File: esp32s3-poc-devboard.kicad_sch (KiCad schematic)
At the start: 12 parts, among them U1 ESP32-S3, U2 AMS1117-3.3, U3 XC6206P332MR

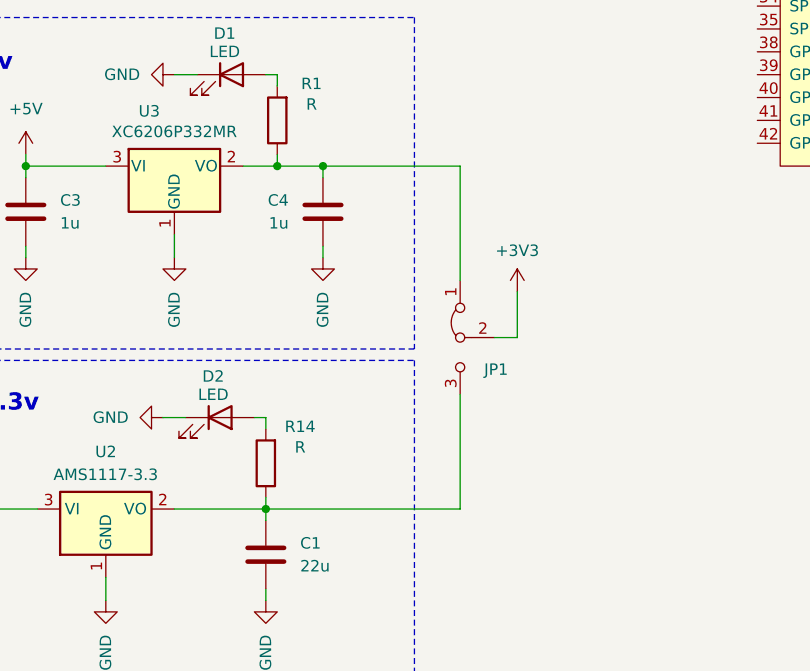
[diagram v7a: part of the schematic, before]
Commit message: remove 3v3 jumper
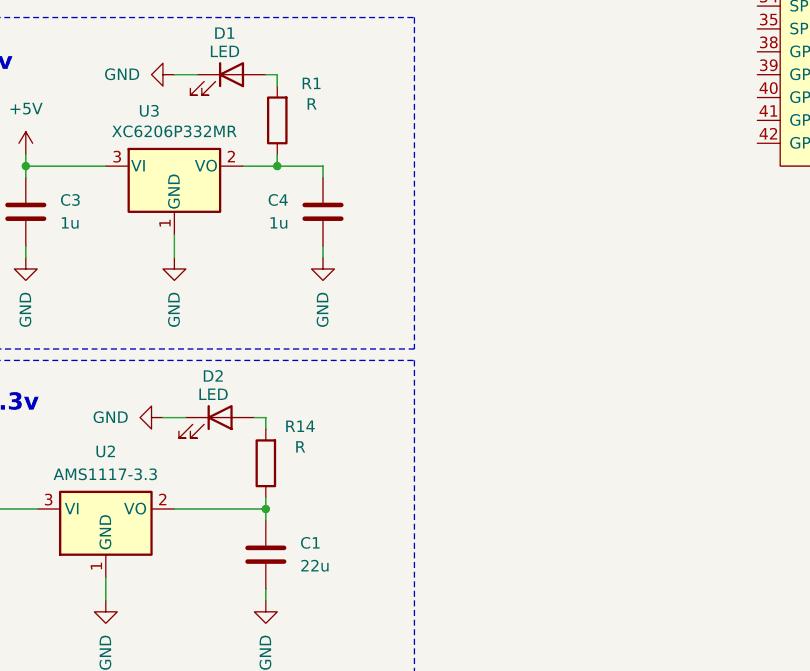
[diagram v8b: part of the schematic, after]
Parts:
- removed JP1: PWR, symbol Jumper:Jumper_3_Bridged12
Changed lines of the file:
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@@
-	)
-	(junction
-		(at 72.39 135.89)
-		(diameter 0)
-		(color 0 0 0 0)
 	)
 	(junction
@@
 	(wire
 		(pts
-			(xy 91.44 154.94) (xy 93.98 154.94)
-		)
-		(stroke
-			(width 0)
-			(type default)
-		)
-	)
-	(wire
-		(pts
-			(xy 93.98 154.94) (xy 93.98 149.86)
-		)
-		(stroke
-			(width 0)
-			(type default)
-		)
-	)
-	(wire
-		(pts
 			(xy 66.04 173.99) (xy 66.04 175.26)
 		)
@@
 	(wire
 		(pts
-			(xy 87.63 148.59) (xy 87.63 135.89)
-		)
-		(stroke
-			(width 0)
-			(type default)
-		)
-	)
-	(wire
-		(pts
 			(xy 29.21 175.26) (xy 29.21 173.99)
 		)
@@
 	(wire
 		(pts
-			(xy 66.04 173.99) (xy 87.63 173.99)
-		)
-		(stroke
-			(width 0)
-			(type default)
-		)
-	)
-	(wire
-		(pts
 			(xy 66.04 125.73) (xy 67.31 125.73)
 		)
@@
 	(wire
 		(pts
-			(xy 72.39 135.89) (xy 87.63 135.89)
-		)
-		(stroke
-			(width 0)
-			(type default)
-		)
-	)
-	(wire
-		(pts
 			(xy 55.88 125.73) (xy 58.42 125.73)
 		)
@@
 		(pts
 			(xy 29.21 173.99) (xy 40.64 173.99)
-		)
-		(stroke
-			(width 0)
-			(type default)
-		)
-	)
-	(wire
-		(pts
-			(xy 87.63 173.99) (xy 87.63 161.29)
 		)
 		(stroke
@@
 	)
 	(symbol
-		(lib_id "Jumper:Jumper_3_Bridged12")
-		(at 87.63 154.94 90)
-		(mirror x)
-		(unit 1)
-		(exclude_from_sim no)
-		(in_bom no)
-		(on_board yes)
-		(dnp no)
-		(property "Reference" "JP1"
-			(at 92.964 158.496 90)
-			(effects
-				(font
-					(size 1.27 1.27)
-				)
-				(justify left)
-			)
-		)
-		(property "Value" "PWR"
-			(at 92.456 159.766 90)
-			(effects
-				(font
-					(size 1.27 1.27)
-				)
-				(justify left)
-				(hide yes)
-			)
-		)
-		(property "Footprint" ""
-			(at 87.63 154.94 0)
-			(effects
-				(font
-					(size 1.27 1.27)
-				)
-				(hide yes)
-			)
-		)
-		(property "Datasheet" "~"
-			(at 87.63 154.94 0)
-			(effects
-				(font
-					(size 1.27 1.27)
-				)
-				(hide yes)
-			)
-		)
-		(property "Description" "Jumper, 3-pole, pins 1+2 closed/bridged"
-			(at 87.63 154.94 0)
-			(effects
-				(font
-					(size 1.27 1.27)
-				)
-				(hide yes)
-			)
-		)
-		(pin "3"
-		)
-		(pin "2"
-		)
-		(pin "1"
-		)
-		(instances
-			(project ""
-				(path "/a6beb550-83d0-4746-bc61-cde76b7466a3"
-					(reference "JP1")
-					(unit 1)
-				)
-			)
-		)
-	)
-	(symbol
 		(lib_id "Device:R")
 		(at 66.04 168.91 180)
@@
 					(unit 1)
 				)
-			)
-		)
-	)
-	(symbol
-		(lib_id "power:+3V3")
-		(at 93.98 149.86 0)
-		(mirror y)
-		(unit 1)
-		(exclude_from_sim no)
-		(in_bom yes)
-		(on_board yes)
-		(dnp no)
-		(property "Reference" "#PWR023"
-			(at 93.98 153.67 0)
-			(effects
-				(font
-					(size 1.27 1.27)
-				)
-				(hide yes)
-			)
-		)
-		(property "Value" "+3V3"
-			(at 93.98 145.288 0)
-			(effects
-				(font
-					(size 1.27 1.27)
-				)
-			)
-		)
-		(property "Footprint" ""
-			(at 93.98 149.86 0)
-			(effects
-				(font
-					(size 1.27 1.27)
-				)
-				(hide yes)
-			)
-		)
-		(property "Datasheet" ""
-			(at 93.98 149.86 0)
-			(effects
-				(font
-					(size 1.27 1.27)
-				)
-				(hide yes)
-			)
-		)
-		(property "Description" "Power symbol creates a global label with name \"+3V3\""
-			(at 93.98 149.86 0)
-			(effects
-				(font
-					(size 1.27 1.27)
-				)
-				(hide yes)
-			)
-		)
-		(pin "1"
-		)
-		(instances
-			(project "esp32s3-poc-devboard"
-				(path "/a6beb550-83d0-4746-bc61-cde76b7466a3"
-					(reference "#PWR023")
-					(unit 1)
-				)
